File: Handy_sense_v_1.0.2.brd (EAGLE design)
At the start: 85 x 130.1 mm, 103 parts, among them K1 JS-M1-9V-4, K2 JS-M1-9V-4, K3 JS-M1-9V-4, K4 JS-M1-9V-4, Q1 600mA/40V, Q2 600mA/40V, Q3 600mA/40V, Q4 600mA/40V, Q5 600mA/40V, Q6 600mA/40V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

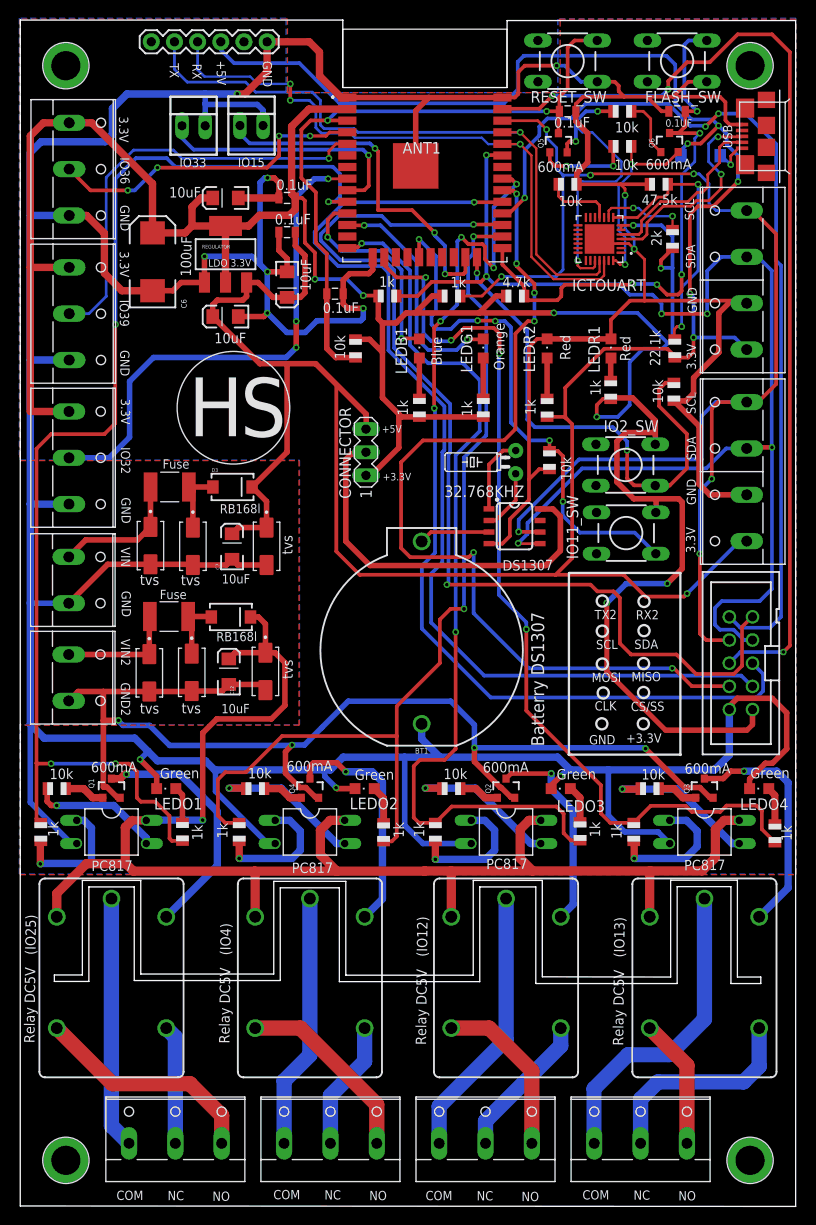
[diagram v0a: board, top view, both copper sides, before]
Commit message: Update version
- change tvs
- add 3.3 V and 5V
- change micro use
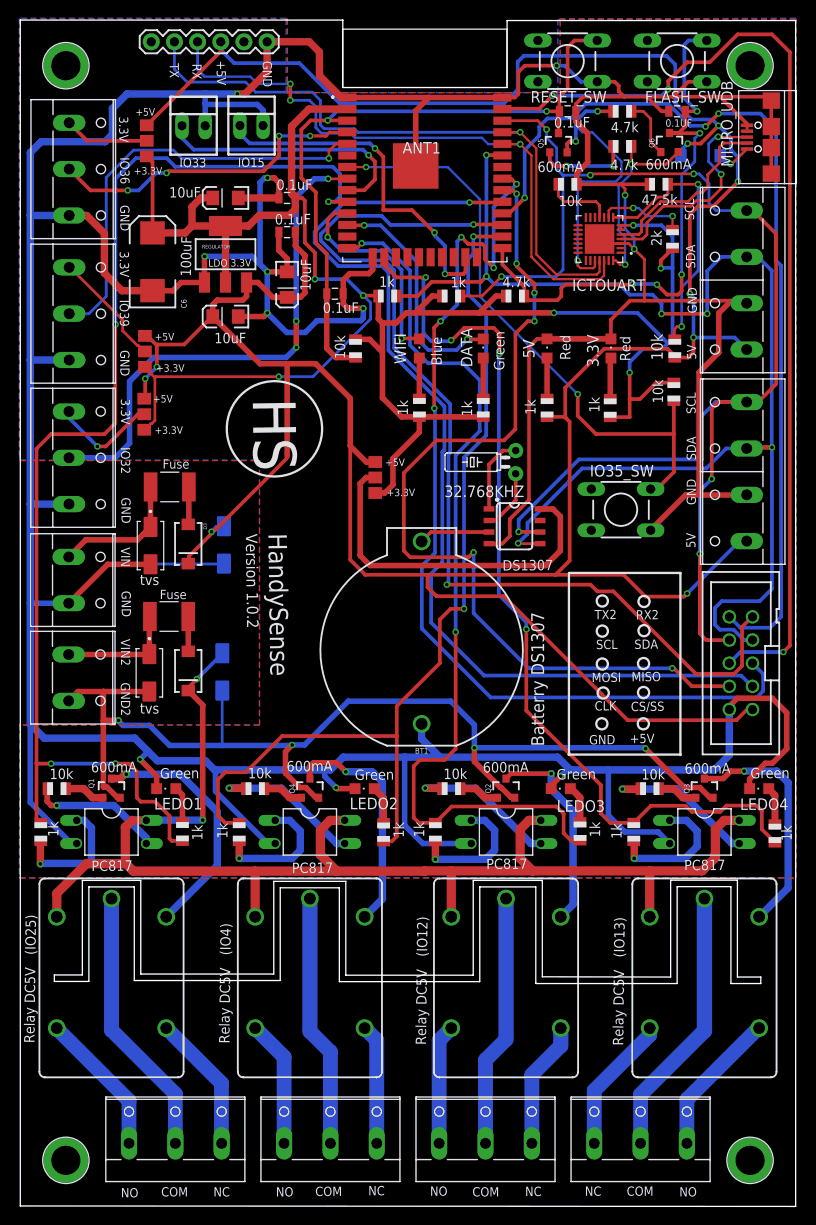
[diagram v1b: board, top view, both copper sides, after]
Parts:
- removed C12, C7: 10uF, SparkFun-Capacitors:EIA3216
- removed CONNECTOR: (no value), con-lstb:MA03-1
- removed IO11_SW, IO2_SW: TACTILE-SWITCH-PTH, GeekAmmo:TAC-SWITCH-PTH
- removed J28CA2, J28CA5: (no value), DIOM505270X240:DIOM505270X240
- removed R27: 10k, adafruit:R0805
- removed USB: MICRO_USB_B_HIROSE_ZX62-B-5PA(11), connector:USB_MICRO_B-HIROSE-ZX62-B-5PA(11)
- added IO35_SW: TACTILE-SWITCH-PTH, GeekAmmo:TAC-SWITCH-PTH
- added JMP1, JMP2, JMP3, JMP4: 0R-JUMPB, jump-0r-smd:B0R-JMP
- added MICRO_UDB: 629105136821, Wurth_Input-Output_Connectors_rev15d:629105136821
- R25, R26: value 10k -> 1k
- R3: value 22.1k -> 10k
- R8, R9: value 10k -> 4.7k
- moved D3 7.91 mm to (18.4, 72.6), turned to 270 degrees
- moved D2 7.54 mm to (18.4, 58.6), turned to 270 degrees
- moved J28CA6 4.72 mm to (22.1, 58.5), flipped to the bottom
- moved J28CA3 4.68 mm to (22.3, 72.5), flipped to the bottom
- moved R1 1.98 mm to (64.7, 87.5)
- renumbered LEDB1 to WIFI, LEDG1 to DATA, LEDR1 to 3.3V, LEDR2 to 5V
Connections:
- new net VA0: JMP2.2, X4.1
- new net VA3: JMP1.2, X5.1
- new net VA6: JMP3.2, X11.1
- net 3.3V: now also JMP1.3, JMP2.3, JMP3.3, JMP4.3, R16.2; no longer CONNECTOR.1, IDC10.1, IO11_SW.3, IO2_SW.3, X11.1, X4.1, X5.1
- net 5V: now also MICRO_UDB.1; no longer USB.1
- net GND: now also IO35_SW.1, MICRO_UDB.4, MICRO_UDB.5, MICRO_UDB.Z1, MICRO_UDB.Z2, MICRO_UDB.Z3, MICRO_UDB.Z4; no longer C7.C, J28CA2.A, R16.1, R27.1, USB.5
- net GND2: no longer C12.C, J28CA5.A
- net IO11: no longer IO11_SW.1, R27.2
- net IO2: no longer IO2_SW.1, R16.2
- net IO35: now also IO35_SW.3, R16.1
- net K1CM: now also X2.2; no longer X2.1
- net K1NC: now also X2.3; no longer X2.2
- net K1NO: now also X2.1; no longer X2.3
- net K2CM: now also X12.2; no longer X12.1
- net K2NC: now also X12.3; no longer X12.2
- net K2NO: now also X12.1; no longer X12.3
- net K3CM: now also X6.2; no longer X6.1
- net K3NC: now also X6.3; no longer X6.2
- net K3NO: now also X6.1; no longer X6.3
- net K4CM: now also X8.2; no longer X8.1
- net K4NC: now also X8.3; no longer X8.2
- net K4NO: now also X8.1; no longer X8.3
- net N$34: no longer J28CA2.C
- net N$37: no longer J28CA5.C
- net RTCVCC: now also JMP4.2; no longer CONNECTOR.2
- net USB_DN: now also MICRO_UDB.2; no longer USB.2
- net USB_DP: now also MICRO_UDB.3; no longer USB.3
- net VIN: now also IDC10.1, JMP1.1, JMP2.1, JMP3.1, JMP4.1; no longer C7.A, CONNECTOR.3
- net VIN2: no longer C12.A
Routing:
- net 3.3V: track 310.7 -> 227.7 mm, vias 8 -> 7
- net VIN: track 288.6 -> 357.4 mm, vias 6 -> 9
- net IO35: track 0.00 -> 66.7 mm, vias 0 -> 2
- net IO11: track 58.8 -> 0.00 mm, vias 5 -> 0
- net IO2: track 55.6 -> 0.00 mm, vias 2 -> 0
- net GND: track 624.5 -> 645.9 mm
- net VIN2: track 163.8 -> 147.8 mm, vias 1 -> 2
- net VA3: track 0.00 -> 12.8 mm
- net VA6: track 0.00 -> 11.7 mm, vias 0 -> 1
- net VA0: track 0.00 -> 9.32 mm
- net K1NO: track 25.1 -> 15.9 mm
- net K4NC: track 23.5 -> 16.0 mm
- net GND2: track 127.5 -> 120.2 mm
- net K2NO: track 21.1 -> 13.9 mm
- net K3NO: track 18.7 -> 13.2 mm
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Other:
- board text added: "5V"
- board text added: "HS"
- board text added: "HandySense"
- board text added: "Version 1.0.2"
- board text removed: "22.1k"
- board text removed: "H"
- board text removed: "Handy Sense board"
- board text removed: "Open Innavation"
- board text removed: "Orange"
- board text removed: "RB168l"
- board text removed: "S"
- board text removed: "Version 1.0"
